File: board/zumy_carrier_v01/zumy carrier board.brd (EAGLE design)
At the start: 90 x 60 mm, 24 parts, among them IC1 SN74AUP2G17, IC2 SN74AUP2G17, J1 ODROID_POWER, J2 BATT_POWER, SW1 500SSP1S1M6QEA

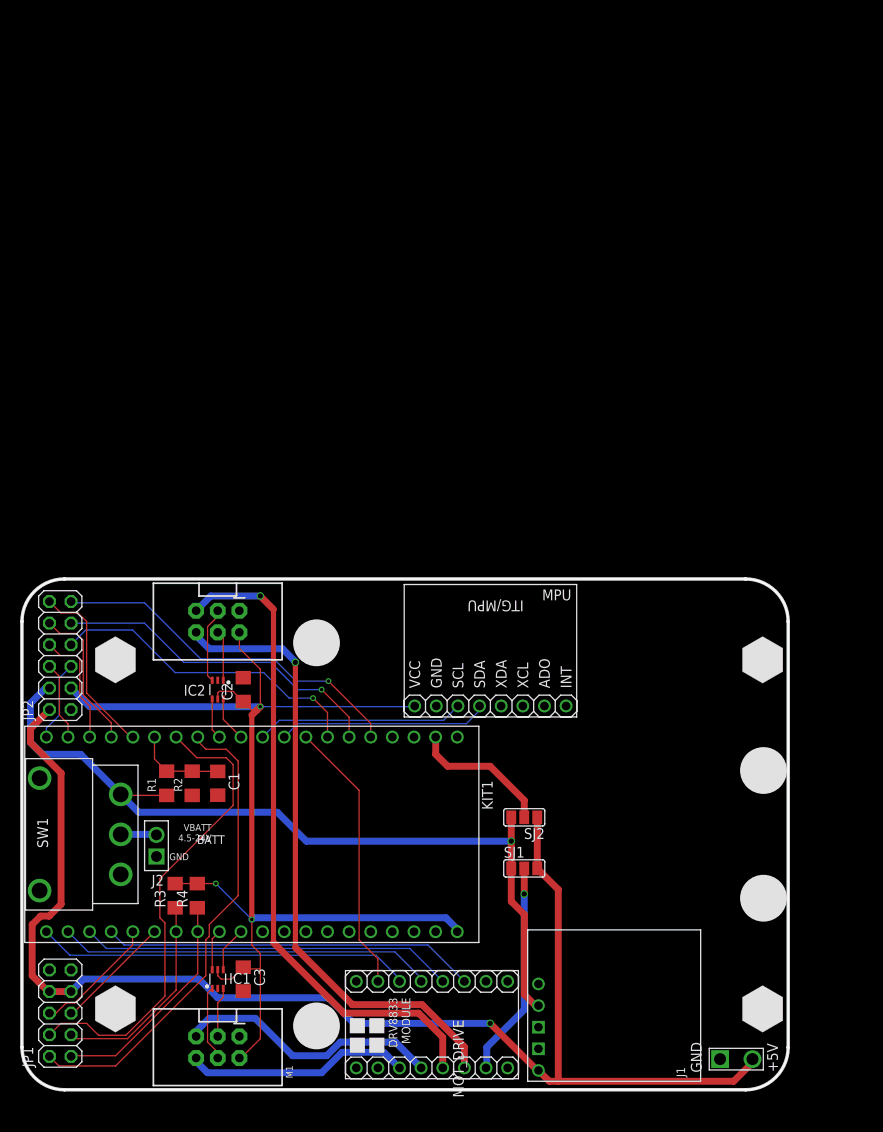
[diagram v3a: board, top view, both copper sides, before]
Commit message: Ready to Test on Othermill
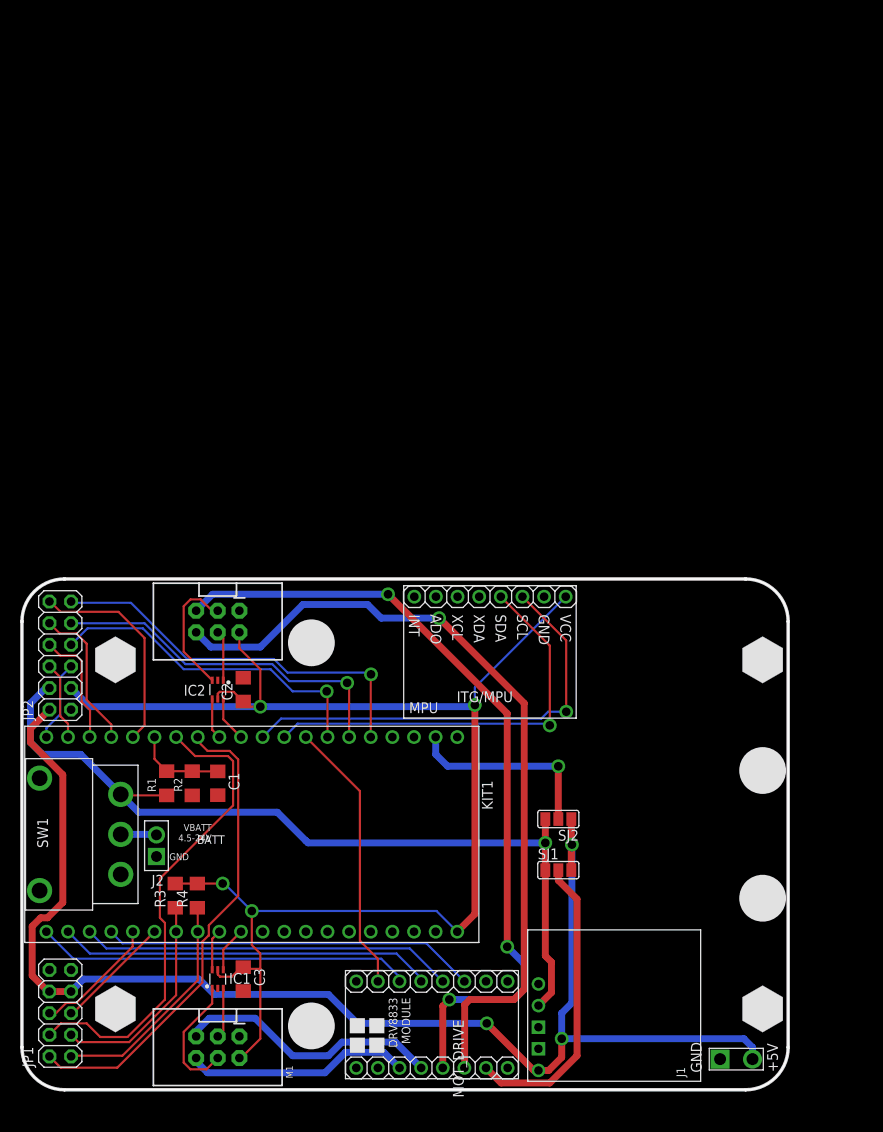
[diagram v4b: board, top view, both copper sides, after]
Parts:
- moved SJ1 4.00 mm to (18.0, -4.20)
- moved SJ2 4.00 mm to (18.0, 1.80)
- moved MPU 3.00 mm to (10.0, 20.0), turned to 0 degrees
- moved U$1 0.60 mm to (-11.0, 22.5)
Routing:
- net MPU_SCL: track 24.5 -> 52.5 mm, vias 0 -> 1
- net +3V3: track 142.9 -> 169.7 mm, vias 3 -> 4
- net MPU_SDA: track 24.8 -> 49.4 mm, vias 0 -> 1
- net M2_OUT1: track 74.1 -> 94.9 mm
- net M2_OUT2: track 77.7 -> 94.0 mm, vias 1 -> 3
- net N$3: track 25.3 -> 35.5 mm, vias 1 -> 0
- net N$1: track 16.7 -> 23.2 mm, vias 0 -> 1
- net M2_EB: track 8.89 -> 15.0 mm
- net M1_EA: track 8.89 -> 15.0 mm
- net MBED_A0: track 21.3 -> 25.2 mm
- net MBED_MOSI: track 42.7 -> 46.2 mm
- net V+: track 97.9 -> 101.2 mm
- net MBED_MISO: track 39.6 -> 41.8 mm
- net MBED_SCK: track 37.7 -> 39.3 mm
- net MBED_SCL: track 24.6 -> 25.3 mm
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
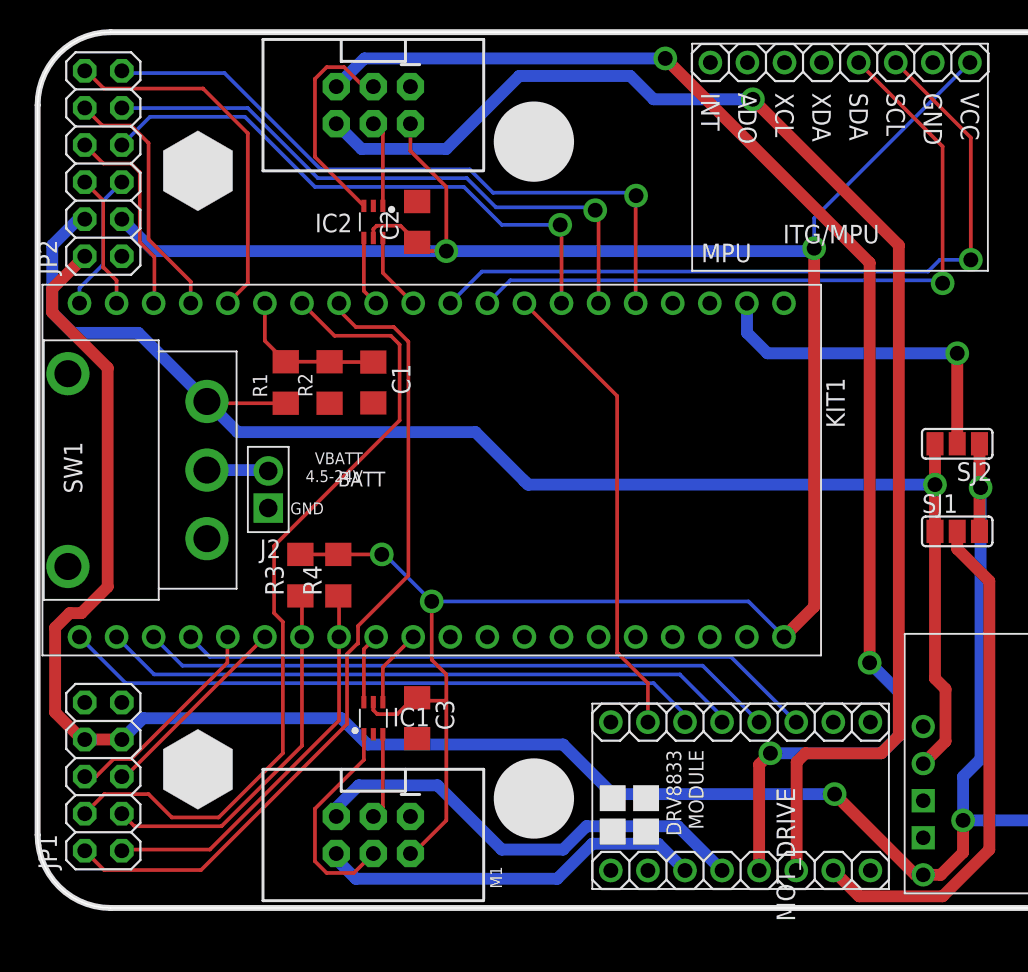
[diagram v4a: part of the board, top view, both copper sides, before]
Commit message: Pulled back switch from edge, just need to fix silkscreen.
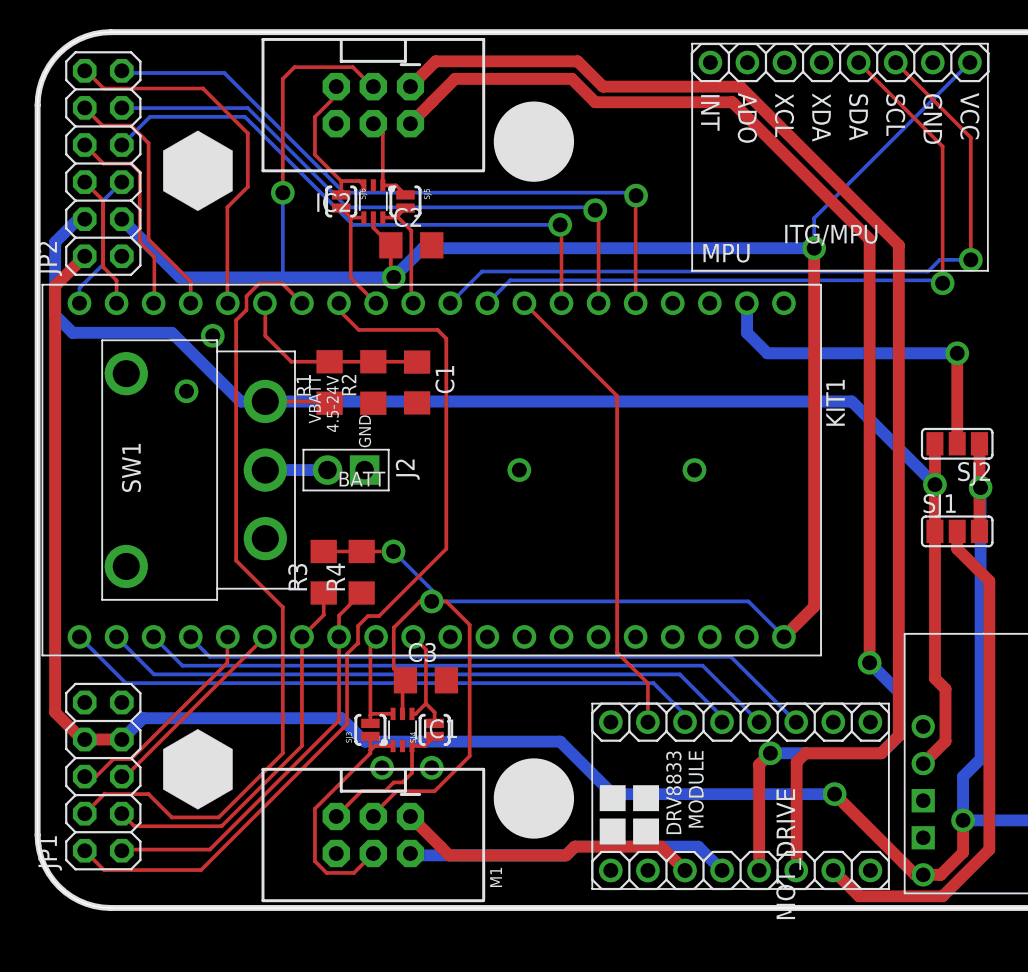
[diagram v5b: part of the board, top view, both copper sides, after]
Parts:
- added SJ3, SJ4, SJ5, SJ6: SOLDERJUMPERNO, SparkFun-Passives:SJ_2S-NO
- moved J2 7.09 mm to (-22.6, 0.00), turned to 180 degrees
- moved SW1 4.00 mm to (-29.4, 0.00)
- moved C1 3.00 mm to (-19.0, 6.00)
- moved R1 3.00 mm to (-25.0, 6.00)
- moved R2 3.00 mm to (-22.0, 6.00)
- moved C3 2.67 mm to (-18.4, -14.4), turned to 0 degrees
- moved IC1 2.15 mm to (-20.0, -17.8)
- moved C2 1.65 mm to (-19.4, 15.4), turned to 0 degrees
- moved R3 1.61 mm to (-25.4, -7.00)
- moved R4 1.61 mm to (-22.8, -7.00)
- moved IC2 1.40 mm to (-22.0, 18.4)
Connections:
- net +3V3: now also M1.3, M2.3; no longer M1.2, M2.2
- net GND: now also M1.6, M2.6; no longer M1.1, M2.1
- net M1_EA: now also SJ3.1
- net M1_EAD: now also SJ3.2
- net M1_EB: now also M1.5, SJ4.1; no longer M1.3
- net M1_EBD: now also SJ4.2
- net M1_OUT1: now also M1.1; no longer M1.6
- net M1_OUT2: now also M1.2; no longer M1.5
- net M2_EA: now also SJ5.1
- net M2_EAD: now also SJ5.2
- net M2_EB: now also M2.5, SJ6.1; no longer M2.3
- net M2_EBD: now also SJ6.2
- net M2_OUT1: now also M2.1; no longer M2.6
- net M2_OUT2: now also M2.2; no longer M2.5
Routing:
- net +3V3: track 169.7 -> 184.9 mm, vias 4 -> 5
- net M1_OUT2: track 31.4 -> 22.3 mm
- net M2_OUT1: track 94.9 -> 88.2 mm, vias 1 -> 0
- net M1_OUT1: track 26.6 -> 20.8 mm
- net M2_EB: track 15.0 -> 10.4 mm
- net MBED_TX: track 56.7 -> 61.0 mm
- net M2_OUT2: track 94.0 -> 89.8 mm, vias 3 -> 2
- net M1_EB: track 5.90 -> 10.1 mm
- net +5V: track 160.1 -> 156.5 mm
- net M2_EBD: track 4.82 -> 8.41 mm
- net M2_EAD: track 5.33 -> 8.22 mm
- net M1_EAD: track 4.82 -> 7.67 mm
- net BATT_SENSE: track 10.6 -> 13.4 mm
- net M1_EBD: track 5.33 -> 7.77 mm
- net MBED_RX: track 56.3 -> 54.3 mm
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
